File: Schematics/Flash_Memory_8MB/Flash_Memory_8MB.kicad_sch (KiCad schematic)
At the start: 3 parts, among them U2 W25Q64JVXGIQ

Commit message: updated crystal oscillator
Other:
- note removed: "QSPI_CS_L"
- note removed: "QSPI_SCLK"
- note removed: "QSPI_SD0"
- note removed: "QSPI_SD1"
- note removed: "QSPI_SD2"
- note removed: "QSPI_SD3"
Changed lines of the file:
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@@
     (stroke (width 0) (type default) (color 0 0 0 0))
   )
-  (text "QSPI_SD3" (at 187.96 82.55 0)
+  (label "QSPI_SD1" (at 187.96 63.5 0)
     (effects (font (size 1.27 1.27)) (justify left bottom))
   )
-  (text "QSPI_SD1" (at 186.69 63.5 0)
+  (label "QSPI_SD2" (at 186.69 86.36 0)
     (effects (font (size 1.27 1.27)) (justify left bottom))
   )
-  (text "QSPI_CS_L" (at 222.25 78.74 0)
+  (label "QSPI_CS_L" (at 222.25 78.74 0)
     (effects (font (size 1.27 1.27)) (justify left bottom))
   )
-  (text "QSPI_SD2" (at 187.96 86.36 0)
+  (label "QSPI_SD0" (at 187.96 67.31 0)
     (effects (font (size 1.27 1.27)) (justify left bottom))
   )
-  (text "QSPI_SCLK" (at 186.69 71.12 0)
+  (label "QSPI_SCLK" (at 186.69 71.12 0)
     (effects (font (size 1.27 1.27)) (justify left bottom))
   )
-  (text "QSPI_SD0" (at 186.69 67.31 0)
+  (label "QSPI_SD3" (at 186.69 82.55 0)
     (effects (font (size 1.27 1.27)) (justify left bottom))
   )

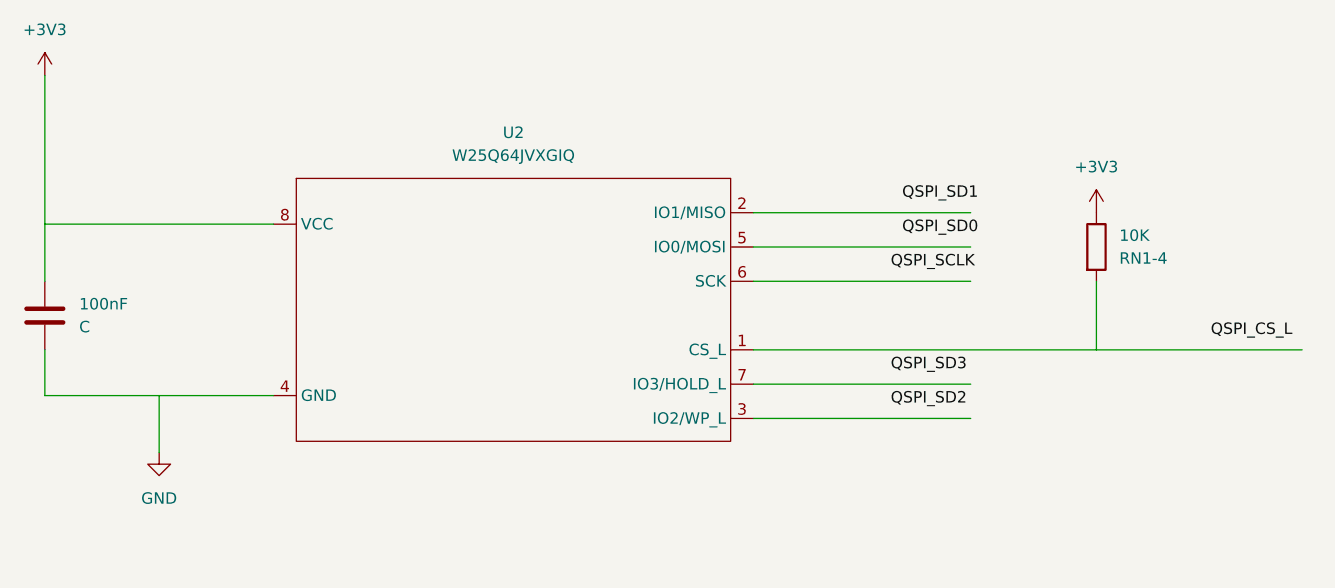
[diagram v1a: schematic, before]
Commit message: updated crystal oscillator and flash memory on module board
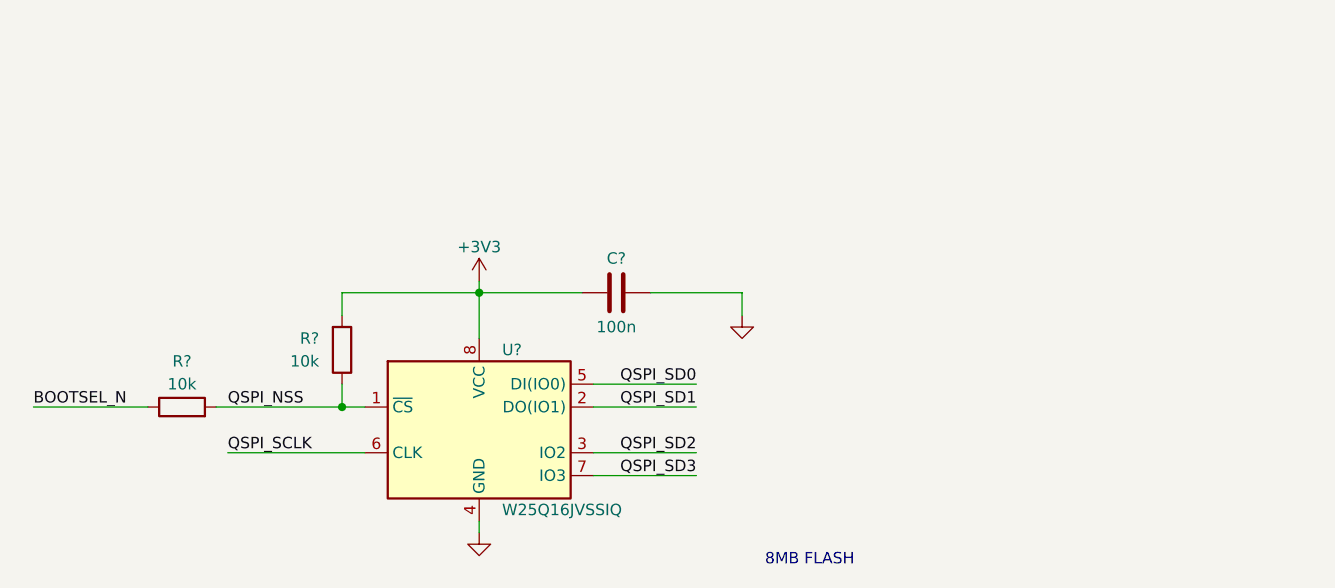
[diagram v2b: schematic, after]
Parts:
- removed 100nF: C, symbol Device:C
- removed 10K: RN1-4, symbol Device:R
- removed U2: W25Q64JVXGIQ, symbol Flash_Memory:W25Q64JVXGIQ
- added C?: 100n, symbol Device:C
- added R? (x2): 10k, symbol Device:R
- added U?: W25Q16JVSSIQ, symbol Merrick_Symbols_KiCad6:W25Q16JVSSIQ
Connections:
- net +3V3: now also C?.1, R?.2, U?.8 (VCC)
- net GND: now also C?.2, U?.4 (GND)
- net QSPI_SCLK: now also U?.6 (CLK)
- net QSPI_SD0: now also U?.5 (DI(IO0))
- net QSPI_SD1: now also U?.2 (DO(IO1))
- net QSPI_SD2: now also U?.3 (IO2)
- net QSPI_SD3: now also U?.7 (IO3)
- new net BOOTSEL_N: R?.1
- new net QSPI_NSS: R?.1, R?.2, U?.1 (~{CS})
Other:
- note added: "8MB FLASH"
